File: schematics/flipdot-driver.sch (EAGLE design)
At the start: 26 parts, among them IC1 4094D, IC10 4094D, IC11 ULN2003AD, IC12 ULN2003AD, IC13 ULN2003AD, IC14 ULN2003AD, IC15 ULN2003AD, IC16 ULN2003AD, IC17 74HC08D, IC18 74HC08D, IC19 74HC02D, IC2 4094D, IC20 74HC14D, IC21 74HC74D, IC3 4094D, IC4 4094D, IC5 4094D, IC6 4094D, IC7 4094D, IC8 4094D, IC9 4094D, Q1 BC808-25SMD

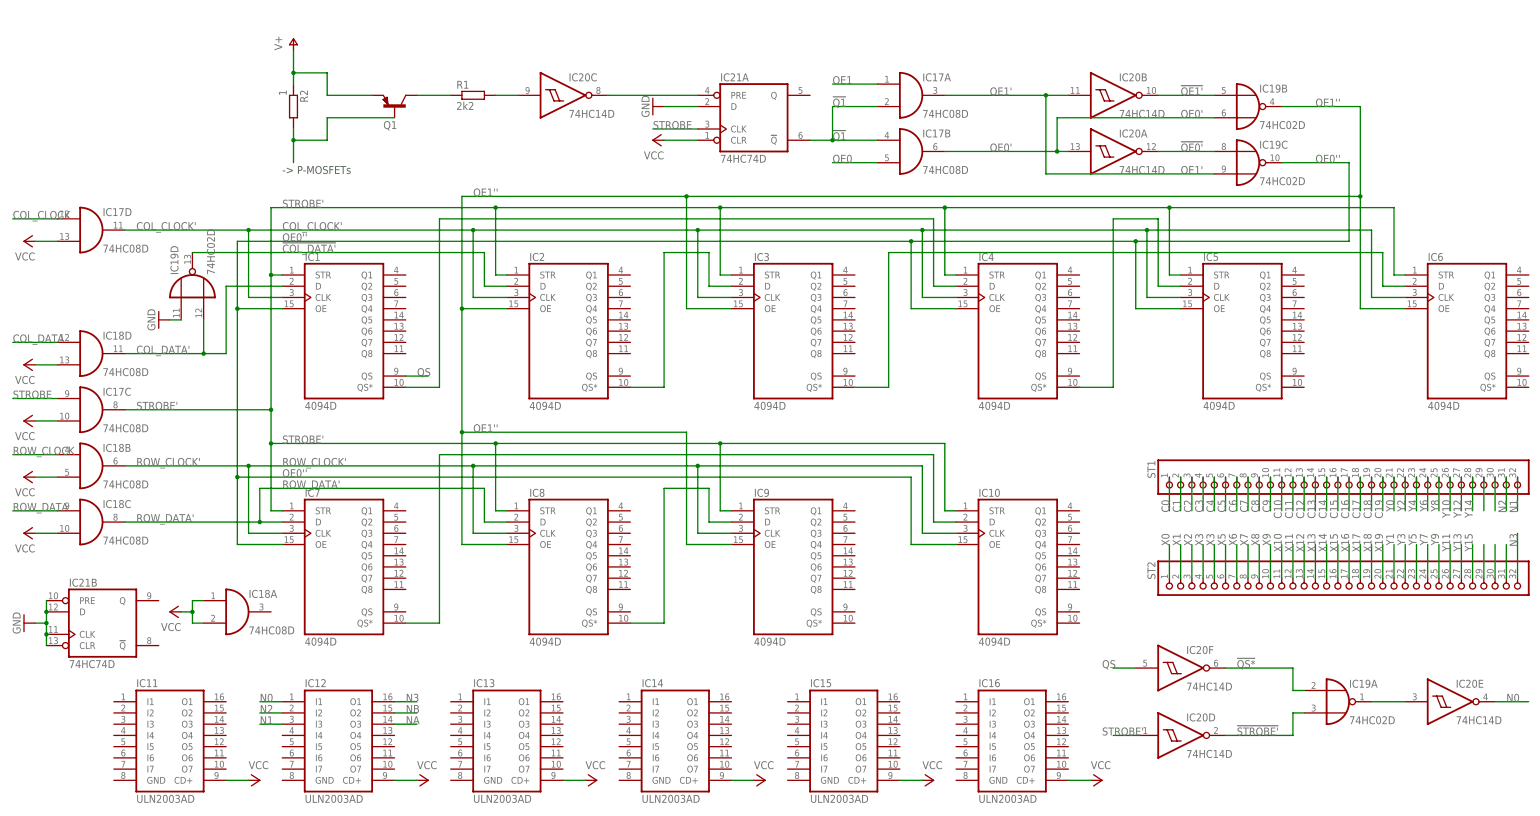
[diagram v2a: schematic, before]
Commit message: net names fixed: Q vs Q1, QS vs QS*
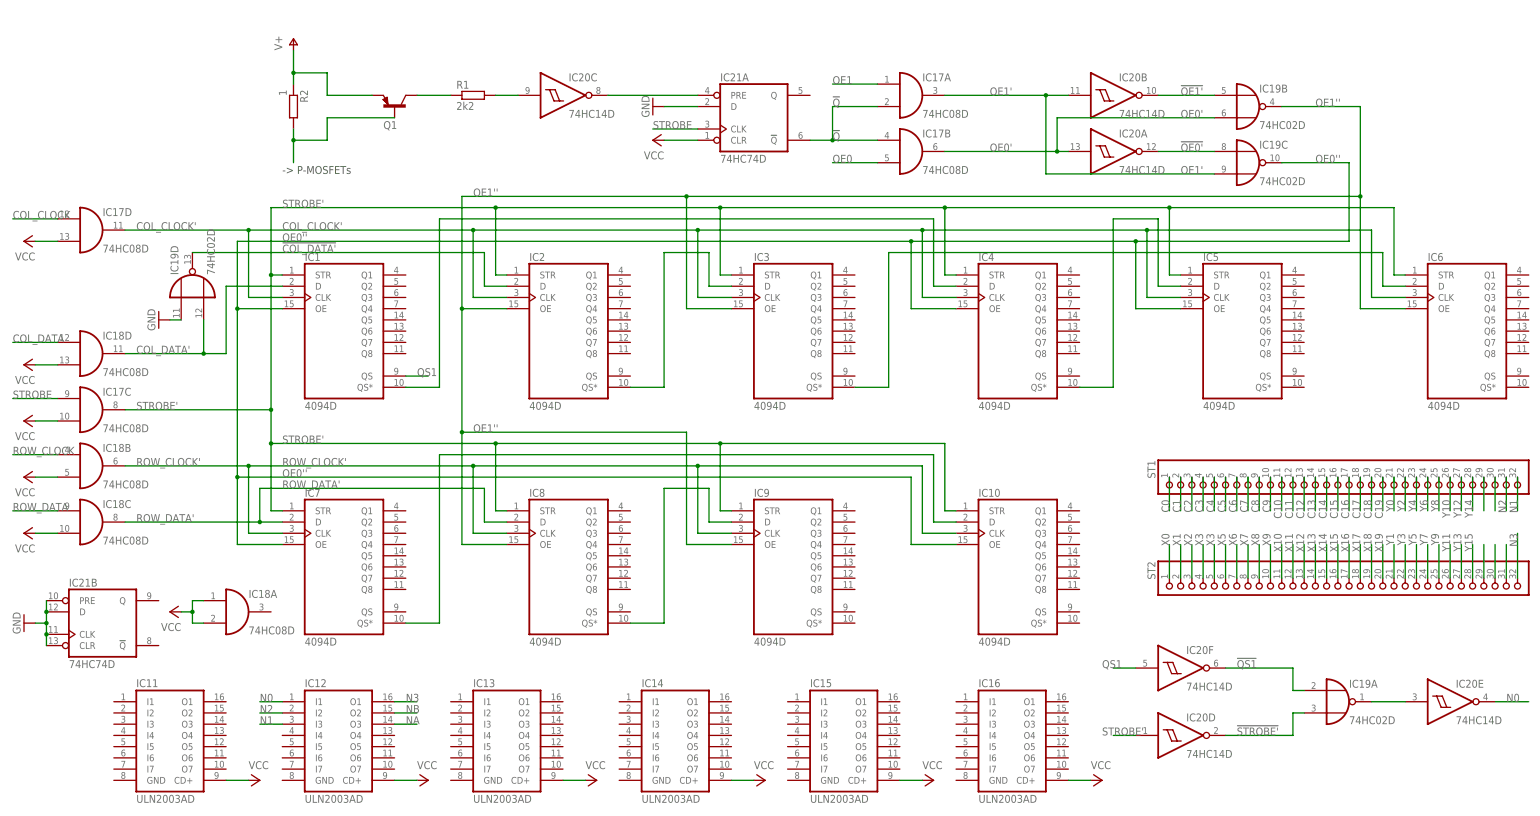
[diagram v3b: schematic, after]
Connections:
- net !Q1 renamed !Q
- net !QS* renamed !QS1
- net QS renamed QS1
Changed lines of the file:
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@@
 <?xml version="1.0" encoding="utf-8"?>
 <!DOCTYPE eagle SYSTEM "eagle.dtd">
-<eagle version="6.4">
+<eagle version="6.5.0">
 <drawing>
 <settings>
@@
 </segment>
 </net>
-<net name="!Q1" class="0">
+<net name="!Q" class="0">
 <segment>
 <pinref part="IC17" gate="B" pin="I0"/>
@@
 </segment>
 </net>
-<net name="!QS*" class="0">
+<net name="!QS1" class="0">
 <segment>
 <pinref part="IC19" gate="A" pin="I0"/>
@@
 </segment>
 </net>
-<net name="QS" class="0">
+<net name="QS1" class="0">
 <segment>
 <pinref part="IC1" gate="A" pin="QS"/>
